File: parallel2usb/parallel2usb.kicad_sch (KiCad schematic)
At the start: 48 parts, among them J1 DB25_Male_MountingHoles, J2 Conn_01x20, J3 Conn_01x03_Male, U1 SN74LVC8T245PW, U2 SN74LVC8T245PW, U3 SN74LVC8T245PW, U4 Pico

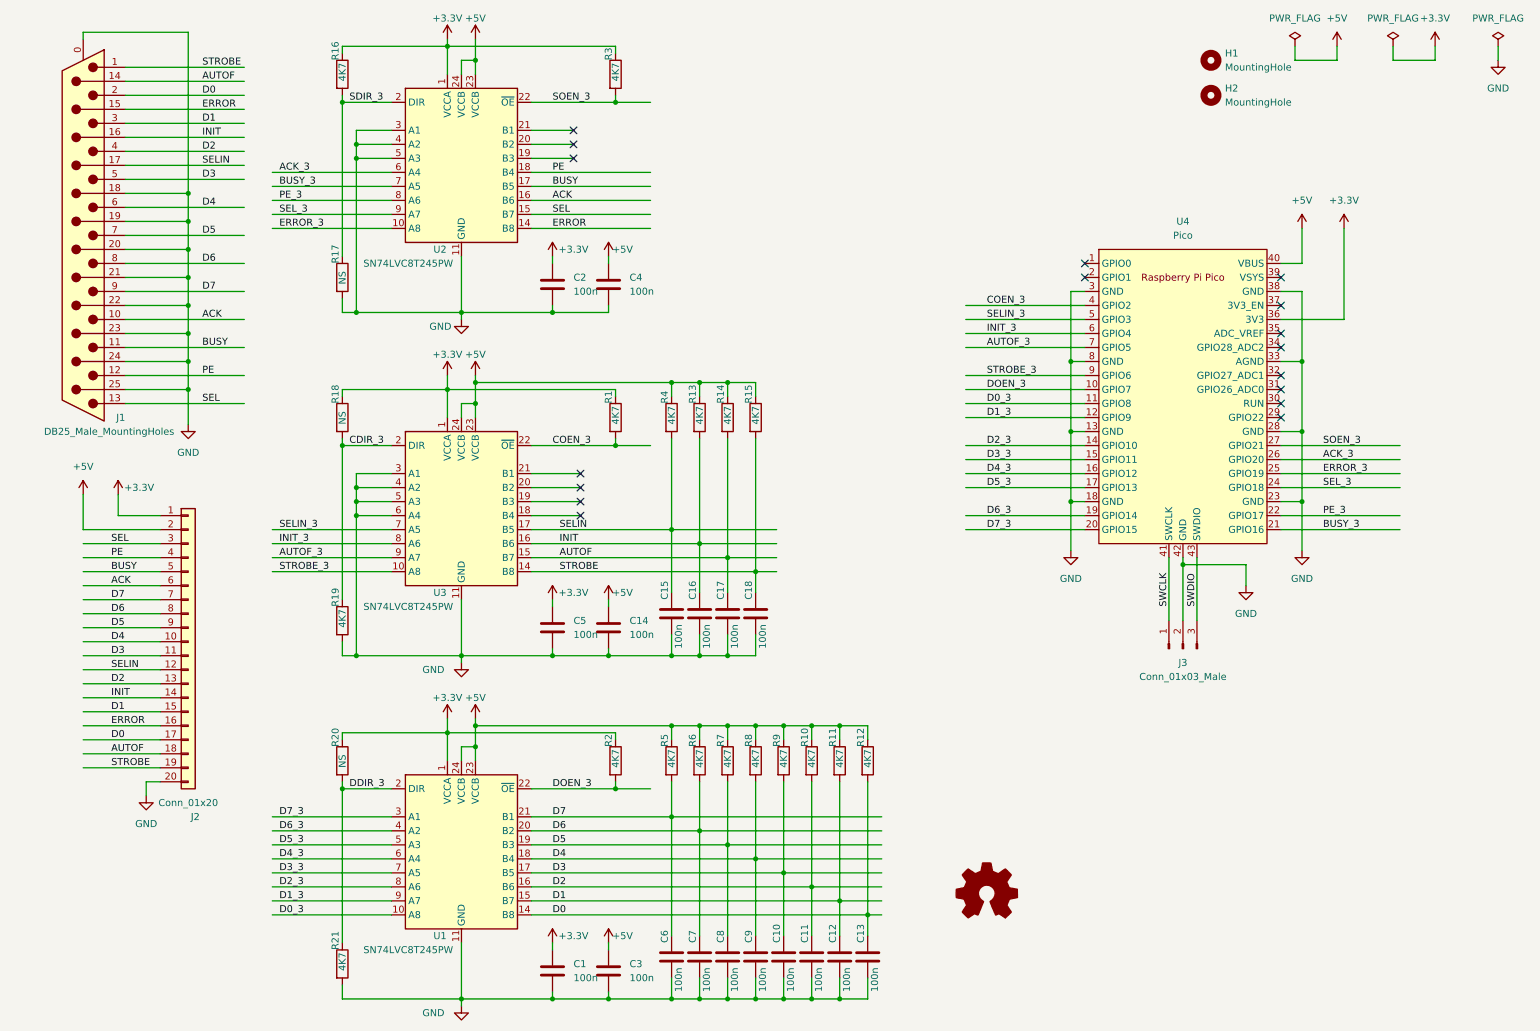
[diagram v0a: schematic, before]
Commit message: Design with 74LVC161284.
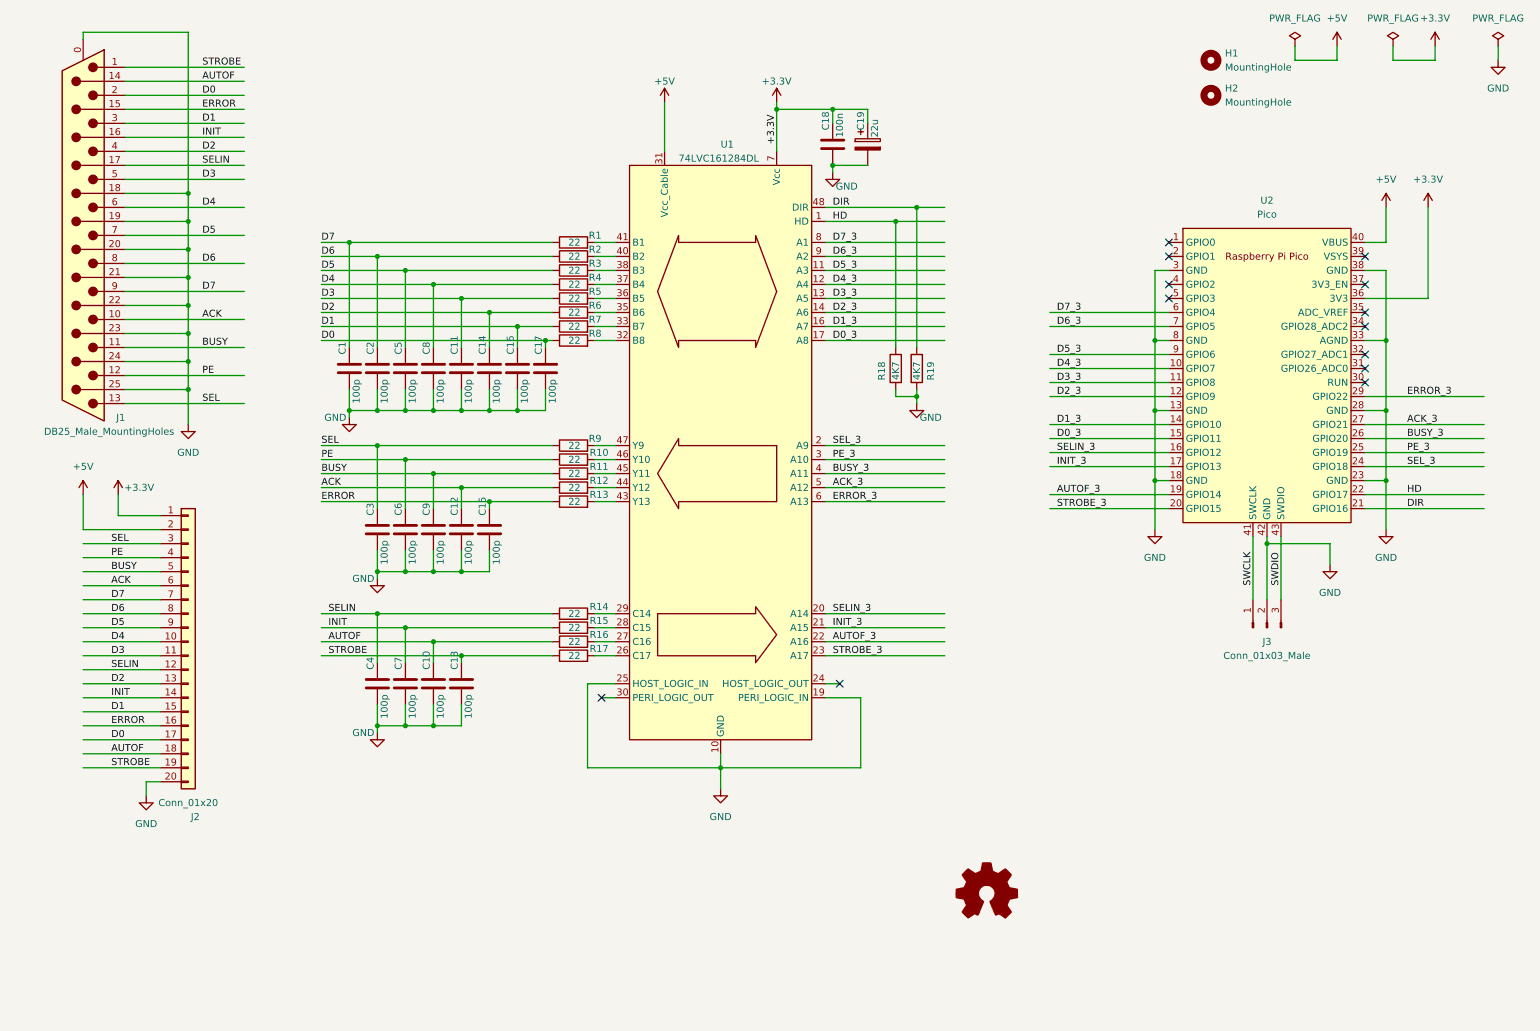
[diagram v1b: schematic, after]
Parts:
- removed R20: NS, Resistor_SMD:R_0603_1608Metric_Pad0.98x0.95mm_HandSolder, symbol Device:R
- removed R21: 4K7, Resistor_SMD:R_0603_1608Metric_Pad0.98x0.95mm_HandSolder, symbol Device:R
- removed U1, U2, U3: SN74LVC8T245PW, Package_SO:TSSOP-24_4.4x7.8mm_P0.65mm, symbol sn74lvc8t245:SN74LVC8T245PW
- added C19: 22u, Capacitor_SMD:C_0603_1608Metric_Pad1.08x0.95mm_HandSolder, symbol Device:C_Polarized
- added U1: 74LVC161284DL, Package_SO:SSOP-48_7.5x15.9mm_P0.635mm, symbol 74lvc161284:74LVC161284DL
- C1, C10, C11, C12, C13, C14, C15, C16, C17, C2, C3, C4, C5, C6, C7, C8, C9: value 100n -> 100p
- R1, R10, R11, R12, R13, R14, R15, R16, R2, R3, R4, R5, R6, R7, R8, R9: value 4K7 -> 22
- R17: value NS -> 22
- R18: value NS -> 4K7
- U2: renamed from U4; footprint Raspberry Pico:RPi_Pico_SMD_TH -> RPi_Pico:RPi_Pico_SMD_TH
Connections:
- net +3.3V: now also C18.1, C19.1, U1.18 (Vcc), U1.7 (Vcc); no longer C1.1, C2.1, C5.1, R1.1, R16.1, R18.1, R2.1, R3.1
- net +5V: now also U1.31 (Vcc_Cable), U1.42 (Vcc_Cable); no longer C14.1, C3.1, C4.1, R10.1, R11.1, R12.1, R13.1, R14.1, R15.1, R4.1, R5.1, R6.1, R7.1, R8.1, R9.1
- net ACK: now also C12.1, R12.1
- net ACK_3: now also U2.27 (GPIO21), U1.5 (A12); no longer U2.26 (GPIO20)
- net AUTOF: now also C10.1, R16.1; no longer C17.1, R14.2
- net AUTOF_3: now also U2.19 (GPIO14), U1.22 (A16); no longer U2.7 (GPIO5)
- net BUSY: now also C9.1, R11.1
- net BUSY_3: now also U2.26 (GPIO20), U1.4 (A11); no longer U2.21 (GPIO16)
- net D0: now also C17.1, R8.1; no longer C13.1, R12.2
- net D0_3: now also U2.15 (GPIO11), U1.17 (A8); no longer U2.11 (GPIO8)
- net D1: now also C16.1, R7.1; no longer C12.1, R11.2
- net D1_3: now also U2.14 (GPIO10), U1.16 (A7); no longer U2.12 (GPIO9)
- net D2: now also C14.1, R6.1; no longer C11.1, R10.2
- net D2_3: now also U2.12 (GPIO9), U1.14 (A6); no longer U2.14 (GPIO10)
- net D3: now also C11.1, R5.1; no longer C10.1, R9.2
- net D3_3: now also U2.11 (GPIO8), U1.13 (A5); no longer U2.15 (GPIO11)
- net D4: now also C8.1, R4.1; no longer C9.1, R8.2
- net D4_3: now also U2.10 (GPIO7), U1.12 (A4); no longer U2.16 (GPIO12)
- net D5: now also C5.1, R3.1; no longer C8.1, R7.2
- net D5_3: now also U2.9 (GPIO6), U1.11 (A3); no longer U2.17 (GPIO13)
- net D6: now also C2.1, R2.1; no longer C7.1, R6.2
- net D6_3: now also U2.7 (GPIO5), U1.9 (A2); no longer U2.19 (GPIO14)
- net D7: now also C1.1, R1.1; no longer C6.1, R5.2
- net D7_3: now also U2.6 (GPIO4), U1.8 (A1); no longer U2.20 (GPIO15)
- net ERROR: now also C15.1, R13.1
- net ERROR_3: now also U2.29 (GPIO22), U1.6 (A13); no longer U2.25 (GPIO19)
- net GND: now also R18.1, R19.1, C19.2, U1.10 (GND), U1.15 (GND), U1.19 (PERI_LOGIC_IN), U1.25 (HOST_LOGIC_IN), U1.34 (GND), U1.39 (GND); no longer R17.2, R19.2
- net INIT: now also C7.1, R15.1; no longer C16.1, R13.2
- net INIT_3: now also U2.17 (GPIO13), U1.21 (A15); no longer U2.6 (GPIO4)
- net PE: now also C6.1, R10.1
- net PE_3: now also U2.25 (GPIO19), U1.3 (A10); no longer U2.22 (GPIO17)
- net SEL: now also C3.1, R9.1
- net SELIN: now also C4.1, R14.1; no longer C15.1, R4.2
- net SELIN_3: now also U2.16 (GPIO12), U1.20 (A14); no longer U2.5 (GPIO3)
- net SEL_3: now also U1.2 (A9)
- net STROBE: now also C13.1, R17.1; no longer C18.1, R15.2
- net STROBE_3: now also U2.20 (GPIO15), U1.23 (A17); no longer U2.9 (GPIO6)
- net CDIR_3 renamed HD
- net HD: now also U2.22 (GPIO17), U1.1 (HD); no longer R19.1
- net COEN_3: no longer names the net of R1.2
- net COEN_3: now also U1.41 (B1); no longer U2.4 (GPIO2)
- net DOEN_3: no longer names the net of R2.2
- net DOEN_3: now also U1.40 (B2); no longer U2.10 (GPIO7)
- net SDIR_3: no longer names the net of R16.2
- net SDIR_3: now also U1.27 (C16); no longer R17.1
- net SOEN_3: no longer names the net of R3.2
- net SOEN_3: now also U1.38 (B3); no longer U2.27 (GPIO21)
- new net: R8.2, U1.32 (B8)
- new net: R11.2, U1.45 (Y11)
- new net: R13.2, U1.43 (Y13)
- new net: R17.2, U1.26 (C17)
- new net: R15.2, U1.28 (C15)
- new net: R14.2, U1.29 (C14)
- new net: R7.2, U1.33 (B7)
- new net: R6.2, U1.35 (B6)
- new net: R5.2, U1.36 (B5)
- new net: R4.2, U1.37 (B4)
- new net: R12.2, U1.44 (Y12)
- new net: R10.2, U1.46 (Y10)
- new net: R9.2, U1.47 (Y9)
- new net DIR: R19.2, U1.48 (DIR), U2.21 (GPIO16)
- no-connect marks 17 -> 13
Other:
- moved on the sheet: J3, U2
